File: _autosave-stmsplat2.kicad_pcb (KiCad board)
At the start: 2 copper layers, 97 parts, among them J1 C11_2X36, J10 Conn_01x03_Male, J11 Conn_01x02_Male, J12 Conn_01x04_Male, J13 Conn_01x04_Male, J14 Conn_01x02, J15 Conn_01x02, J16 Screw_Terminal_01x03, J17 Screw_Terminal_01x02, J2 C12_2X36, J3 Conn_01x04_Male, J4 Conn_01x04_Male, J5 Conn_Coaxial, J6 Conn_01x06, J7 Conn_01x04_Male, J8 Conn_01x04_Male, J9 Conn_01x03_Male, Q1 BSS138LT1G, U1 ublox_chinese_PCB_module, U10 XCVR_E30-400M20S, U2 ESP32-C3-13, U3 SST25VF032B, U4 48L512-48LM01, U5 Opamp_Quad_MCP6024, U6 E180-ZG120A, U7 AZ1084C, U8 MCP6S93-X_UN, U9 DS2485

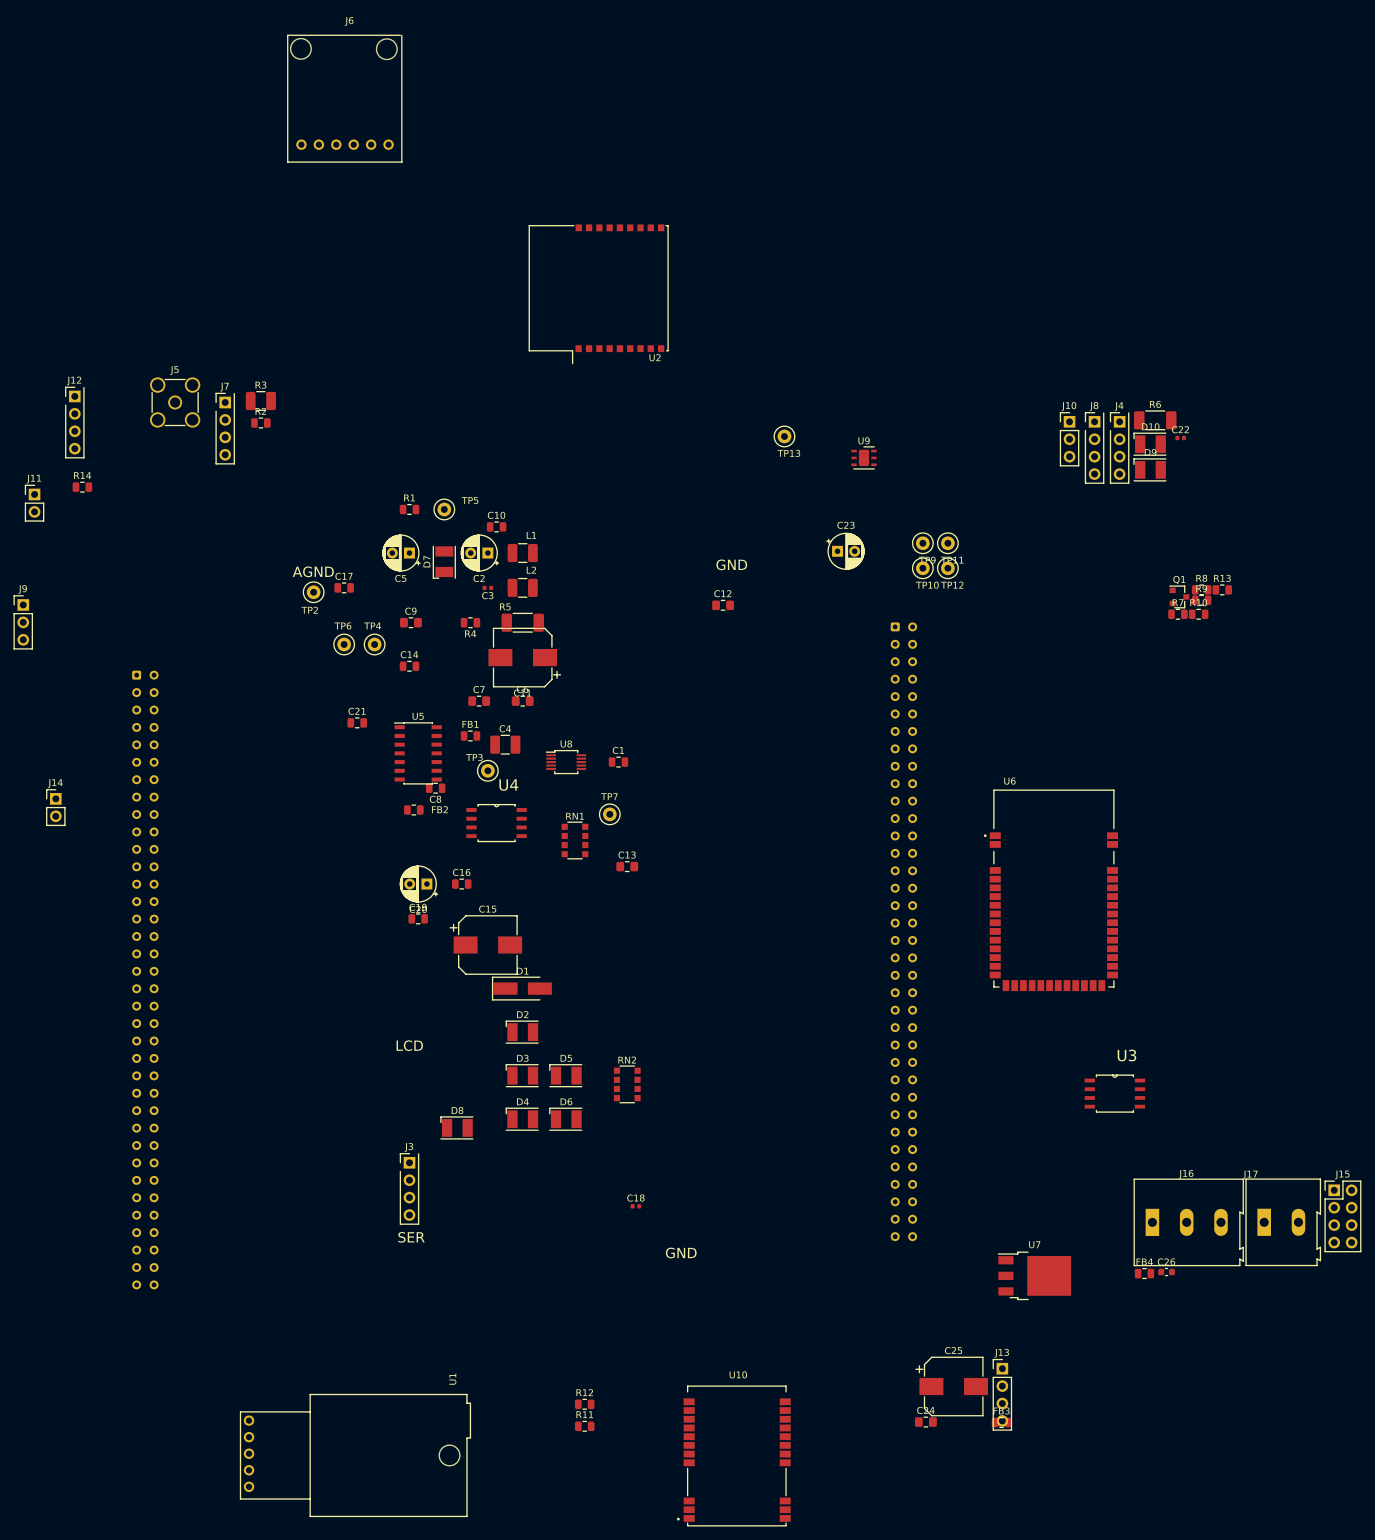
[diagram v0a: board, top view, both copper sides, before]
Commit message: Footprints to new format and all link to the custom splat2footprints library
VER 0.07: ALMOST FROZEN -  pretty library footprints,
3115 footprint unfinished and
changed from J to U designation on SCH
Added com breakout header
labeled raw5v and rawgnd
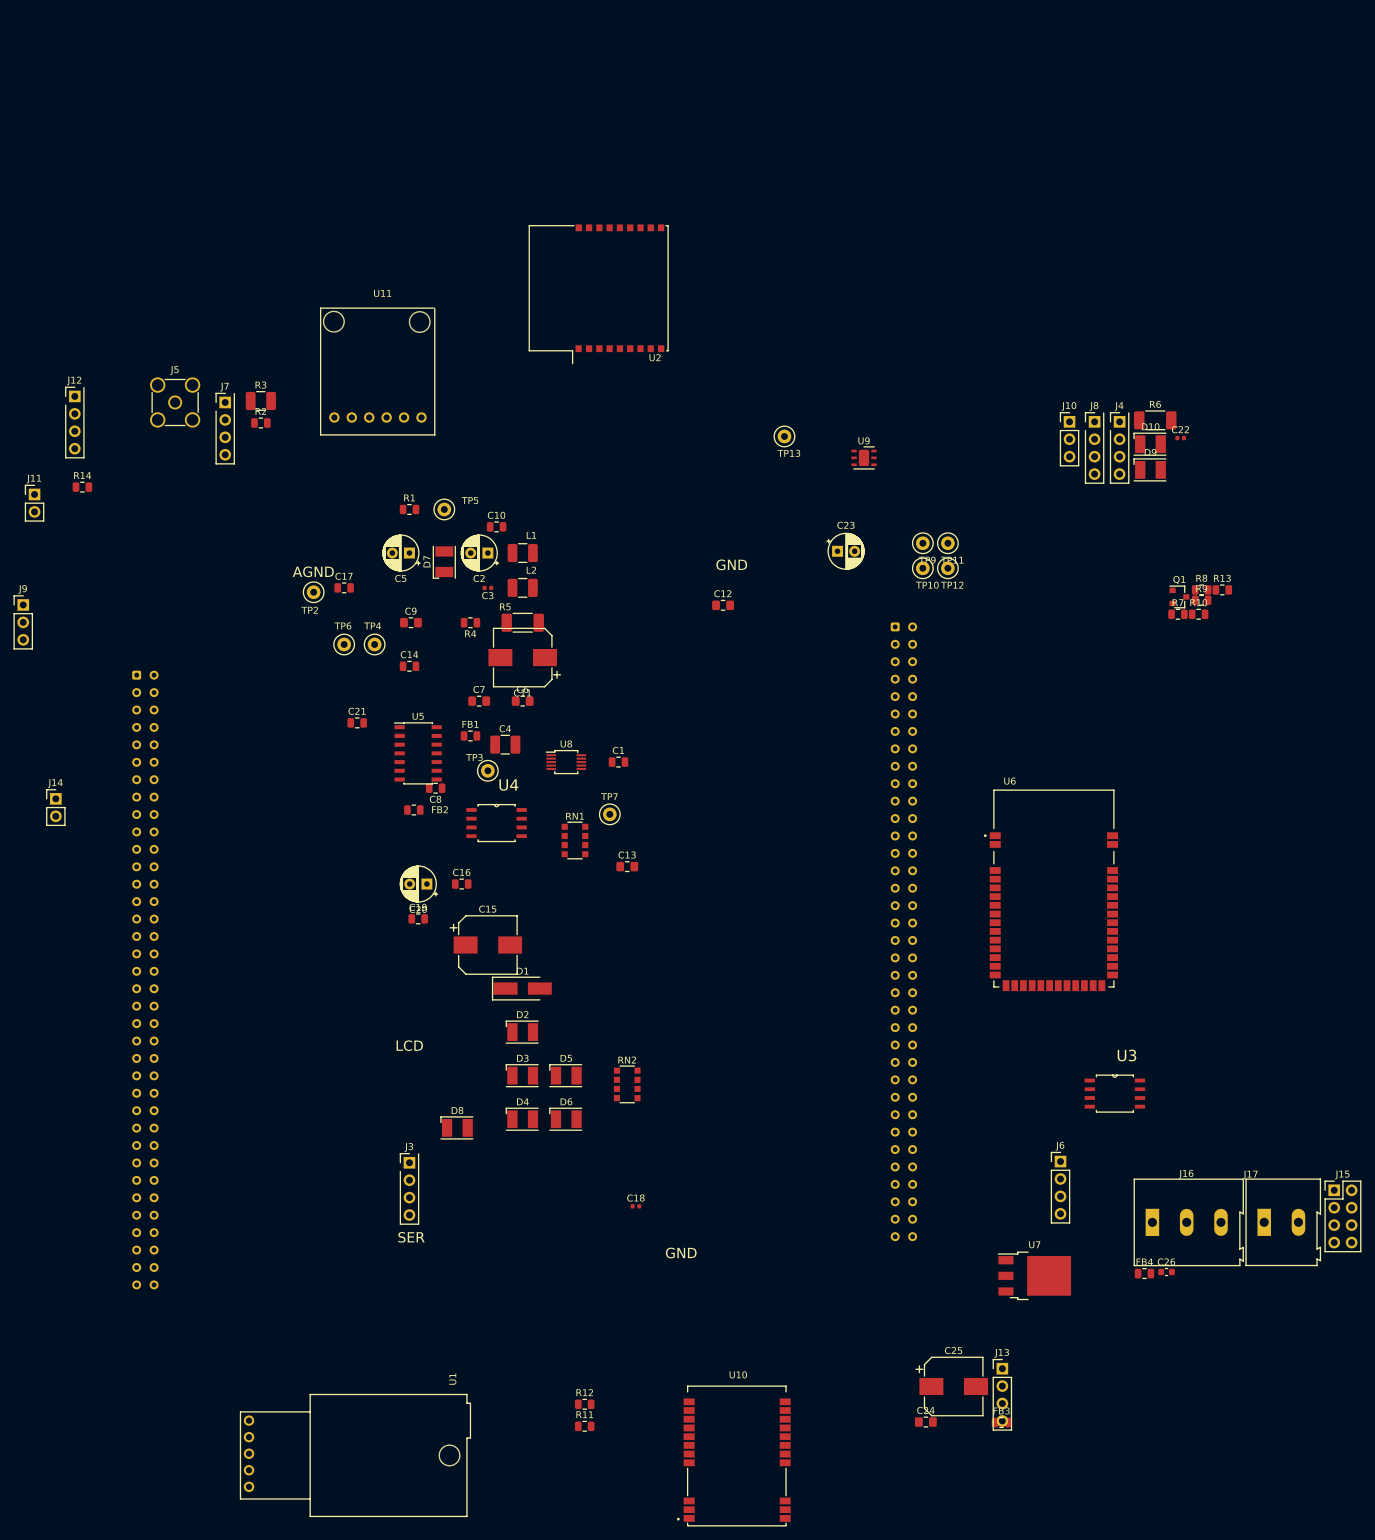
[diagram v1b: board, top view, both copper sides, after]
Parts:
- added U11: 3115_module, splat2footprints:3115_PRESSURE_MODULE, F.Cu at (61.0, 7.72)
- J6: value Conn_01x06 -> Conn_01x04_Male; footprint splat2footprints:3115_PRESSURE_MODULE -> PinHeader_1x04_P2.54mm_Vertical
- U2: value ESP32-C3-13 -> ESP-C3-13U
- moved J6 198.8 mm to (168.6, 131.9)
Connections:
- net /A3V3 renamed A3V3
- net /AGND renamed GNDA
- net /NC renamed NC
- net /PA3 renamed PA3
- net /PA4 renamed PA4
- net /PB1 renamed PB1
- net /PB12 renamed PB12
- net /PB15 renamed PB15
- net /PB2 renamed PB2
- net /PB4 renamed PB4
- net /PB5 renamed PB5
- net /PB8 renamed PB8
- net /PC10 renamed PC10
- net /PC12 renamed PC12
- net /PC2 renamed PC2
- net /PC3 renamed PC3
- net /PC9 renamed PC9
- net /PD1 renamed PD1
- net /PD11 renamed PD11
- net /PD12 renamed PD12
- net /PD13 renamed PD13
- net /PD14 renamed PD14
- net /PD15 renamed PD15
- net /PD3 renamed PD3
- net /PD5 renamed PD5
- net /PD6 renamed PD6
- net /PE0 renamed PE0
- net /PE1 renamed PE1
- net /PE10 renamed PE10
- net /PE11 renamed PE11
- net /PE12 renamed PE12
- net /PE14 renamed PE14
- net /PE15 renamed PE15
- net /PE2 renamed PE2
- net /PE3 renamed PE3
- net /PE5 renamed PE5
- net /PE6 renamed PE6
- net /PE7 renamed PE7
- net /PE8 renamed PE8
- net /PF0 renamed PF0
- net /PF1 renamed PF1
- net /PF11 renamed PF11
- net /PF12 renamed PF12
- net /PF13 renamed PF13
- net /PF2 renamed PF2
- net /PF7 renamed PF7
- net /PF9 renamed PF9
- net /PG0 renamed PG0
- net /PG1 renamed PG1
- net /PG10 renamed PG10
- net /PG12 renamed PG12
- net /PG15 renamed PG15
- net /PG2 renamed PG2
- net /PG3 renamed PG3
- net /PG4 renamed PG4
- net /PG5 renamed PG5
- net /PG8 renamed PG8
- net /XB_PIO4 renamed Net-(RN1-Pad7)
- net Net-(C24-Pad2) renamed /RAWGND
- net Net-(C9-Pad1) renamed /RAW5V
- C1 pad 1: /VDD -> VDD
- C10 pad 1: /E5V -> +5V
- C11 pad 1: /+5V -> +5V
- C13 pad 1: /VDD -> VDD
- C14 pad 2: /VDD -> VDD
- C15 pad 1: /VDD -> VDD
- C16 pad 2: /VDD -> VDD
- C17 pad 2: /VDD -> VDD
- C18 pad 1: /VDD -> VDD
- C19 pad 2: /VDD -> VDD
- C2 pad 1: /VDD -> VDD
- C20 pad 1: /VDD -> VDD
- C21 pad 2: /VDD -> VDD
- C24 pad 1: /VDD -> VDD
- C3 pad 1: /VDD -> VDD
- FB1 pad 2: /E5V -> +5V
- FB2 pad 1: /VDD -> VDD
- J1 pad 18: /+5V -> +5V
- J1 pad 2: /PC11 -> PC11
- J1 pad 28: /PA0 -> PA0
- J1 pad 48: /PE4 -> PE13
- J1 pad 5: /VDD -> VDD
- J1 pad 6: /E5V -> +5V
- J1 pad 63: /PG9 -> PG9
- J12 pad 1: /VDD -> VDD
- J13 pad 1: /VDD -> VDD
- J16 pad 2: /VDD -> VDD
- J2 pad 11: /PA5 -> PA5
- J2 pad 17: /PB6 -> PB6
- J2 pad 2: /PC8 -> PC8
- J2 pad 25: /PB10 -> PA5
- J2 pad 4: /PC6 -> PC6
- J2 pad 5: /PB9 -> PB9
- J2 pad 55: /PE13 -> PE13
- J2 pad 61: /PG14 -> PE13
- J3 pad 1: /+5V -> +5V
- J4 pad 1: /VDD -> VDD
- J6 pad 1: /PB9 -> PC11
- J6 pad 2: /PC8 -> PA0
- J6 pad 3: /PB9 -> PG9
- J6 pad 4: /PB6 -> PC6
- J7 pad 1: /VDD -> VDD
- J8 pad 1: /+5V -> +5V
- Q1 pad 3: /VDD -> VDD
- R1 pad 1: /VDD -> VDD
- R1 pad 2: /PA5 -> PA5
- R11 pad 1: /VDD -> VDD
- R13 pad 1: /VDD -> VDD
- R14 pad 1: /VDD -> VDD
- R4 pad 1: /VDD -> VDD
- RN1 pad 5: /VDD -> VDD
- RN1 pad 6: /VDD -> VDD
- U1 pad 1: /VDD -> VDD
- U1 pad 5: /PA5 -> PA5
- U10 pad 19: /PE13 -> PE13
- U10 pad 9: /VDD -> VDD
- U2 pad 1: /VDD -> VDD
- U2 pad 10: /PE13 -> PE13
- U2 pad 11: /PC6 -> PC6
- U2 pad 12: /PG9 -> PG9
- U3 pad 8: /VDD -> VDD
- U4 pad 8: /VDD -> VDD
- U6 pad 11: /PC11 -> PC11
- U6 pad 12: /PA0 -> PA0
- U6 pad 13: /PC11 -> PC11
- U6 pad 3: /VDD -> VDD
- U7 pad 2: /VDD -> VDD
- U7 pad 3: /+5V -> +5V
- U9 pad 4: /PB6 -> PB6
- U9 pad 5: /PB9 -> PB9
- U9 pad 6: /VDD -> VDD
